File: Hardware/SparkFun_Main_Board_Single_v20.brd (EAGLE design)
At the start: 86.4 x 73.7 mm, 128 parts, among them J1 MICROMOD-2222-C, J10 MICRO-SD-PUSH-PUSH-EXT-PIN, J2 Vertical Qwiic Connector, J4 QWIIC_RIGHT_ANGLE, J5 CORTEX_JTAG_DEBUG_MINIMUM_PTH, J6 MICROMOD_FUNCTION_MAIN, Q1 3.1A/30V/105mΩ, Q2 20V/4.2A/52mΩ/1.4W, U1 STG3856QTR, U2 MCP73831, U3 ESD Diode, U4 AP7347DQ-33W5-7K-3.3V, U5 AP7361C-33

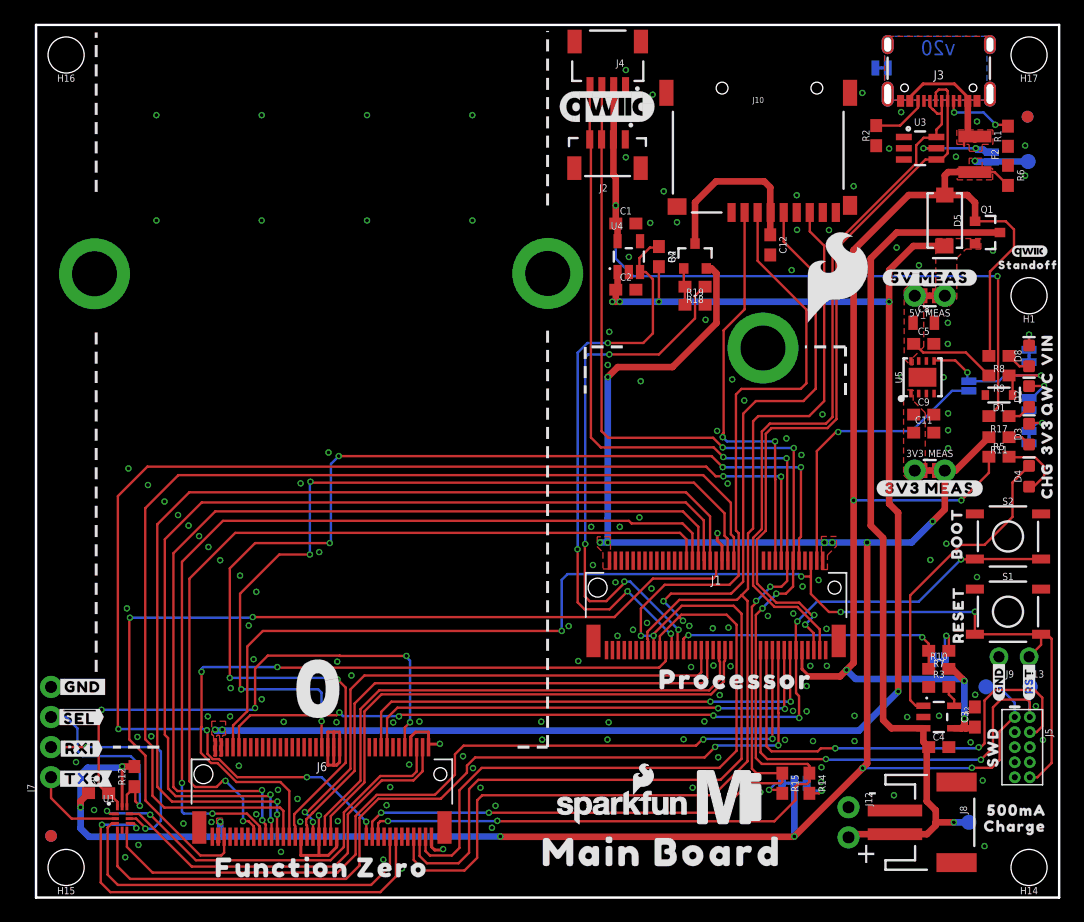
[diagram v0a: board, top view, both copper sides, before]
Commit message: Routes PWM1 pin to power enable pin on function card
* Rolls version to v21
* Fixes PTC silk
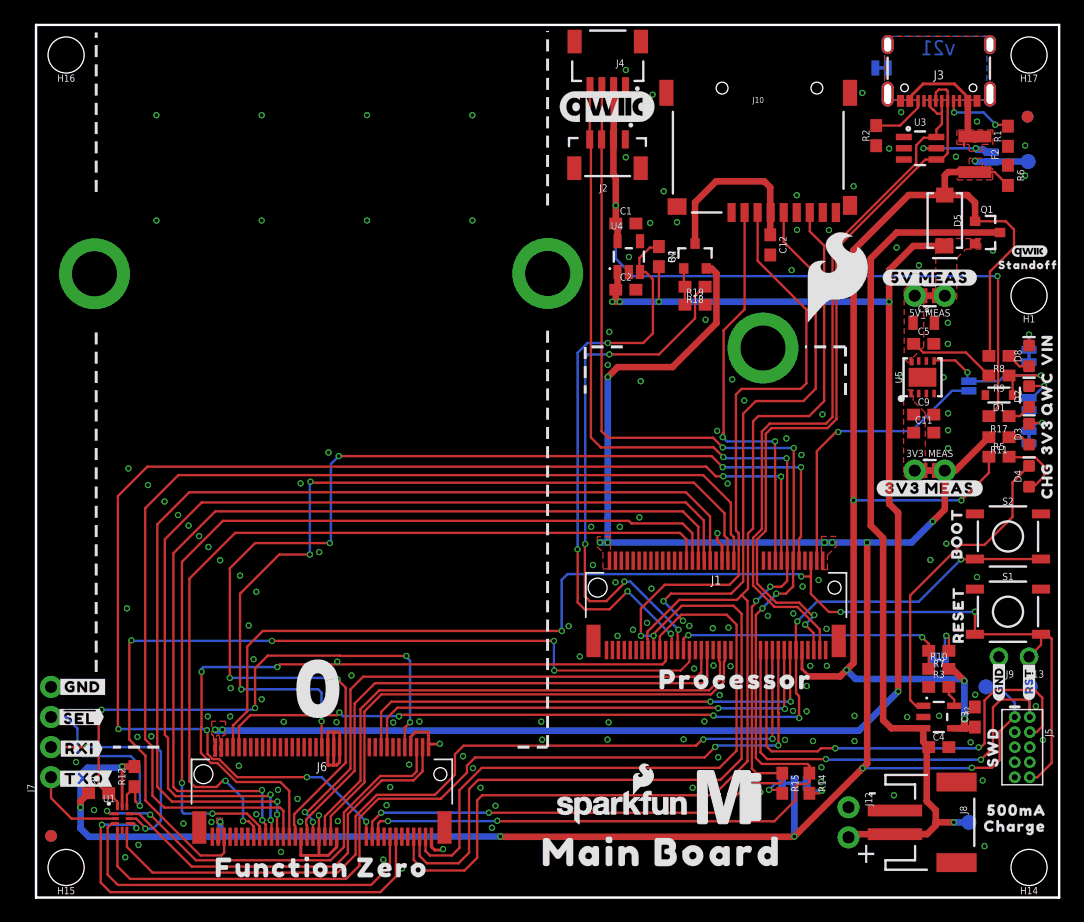
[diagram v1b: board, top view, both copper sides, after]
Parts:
- U$3: device top:#PTC#503 -> top:#PTC#15
- moved U$3 5.79 mm to (77.7, 62.5)
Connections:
- net PWR_EN0: now also J1.47; no longer J1.38
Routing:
- net PWR_EN0: track 78.2 -> 75.1 mm, vias 2 -> 4
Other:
- board text added: "v21"
- board text removed: "v20"
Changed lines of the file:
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@@
 <layer number="28" name="bValues" color="7" fill="1" visible="no" active="yes"/>
 <layer number="29" name="tStop" color="7" fill="3" visible="no" active="yes"/>
-<layer number="30" name="bStop" color="7" fill="6" visible="no" active="yes"/>
+<layer number="30" name="bStop" color="7" fill="6" visible="yes" active="yes"/>
 <layer number="31" name="tCream" color="7" fill="4" visible="no" active="yes"/>
 <layer number="32" name="bCream" color="7" fill="5" visible="no" active="yes"/>
@@
 <wire x1="0" y1="0" x2="0" y2="73.66" width="0.2032" layer="20"/>
 <wire x1="86.36" y1="0" x2="86.36" y2="73.66" width="0.2032" layer="20"/>
-<text x="76.1492" y="71.7296" size="1.27" layer="16" font="vector" ratio="15" rot="MR180" align="center">v20</text>
+<text x="76.1492" y="71.7296" size="1.27" layer="16" font="vector" ratio="15" rot="MR180" align="center">v21</text>
 <text x="43.18" y="-25.654" size="1.778" layer="51" font="vector">Elias Santistevan</text>
 <text x="50.673" y="-14.859" size="1.778" layer="47" font="vector" ratio="15" rot="R180">Units in Inches</text>
@@
 </element>
 <element name="U$27" library="top" package="CHARGE501" value="" x="82.6262" y="6.0198" smashed="yes"/>
-<element name="U$3" library="top" package="#PTC#503" value="" x="83.5152" y="62.5602" smashed="yes" rot="MR0"/>
 <element name="U$7" library="top" package="#SHLD#501" value="" x="74.8792" y="70.0532" smashed="yes" rot="MR0"/>
 <element name="5V_MEAS" library="SparkFun-Jumpers" package="COMBO-JUMPER_2_NC_TRACE" value="JUMPER-COMBO_2_NC_TRACE" x="75.438" y="50.8" smashed="yes" rot="R180">
@@
 <element name="U$20" library="bot" package="#RXI#4" value="" x="3.683" y="12.573" smashed="yes" rot="MR0"/>
 <element name="U$28" library="bot" package="#TXO#5" value="" x="4.064" y="10.033" smashed="yes" rot="MR0"/>
+<element name="U$3" library="top" package="#PTC#15" value="" x="77.724" y="62.484" smashed="yes" rot="MR0"/>
 </elements>
 <signals>
@@
 <via x="25.4762" y="6.4516" extent="1-16" drill="0.3048"/>
 <via x="22.3012" y="6.4008" extent="1-16" drill="0.3048"/>
-<via x="45.7708" y="19.9644" extent="1-16" drill="0.3048"/>
+<via x="45.8978" y="20.3454" extent="1-16" drill="0.3048"/>
 <via x="17.9578" y="22.9616" extent="1-16" drill="0.3048"/>
 <via x="16.4338" y="17.6784" extent="1-16" drill="0.3048"/>
@@
 <via x="7.6708" y="24.4094" extent="1-16" drill="0.3048"/>
 <via x="25.4254" y="19.9136" extent="1-16" drill="0.3048"/>
-<via x="55.2958" y="19.4564" extent="1-16" drill="0.3048"/>
+<via x="55.5498" y="19.3294" extent="1-16" drill="0.3048"/>
 <via x="8.64508125" y="4.445" extent="1-16" drill="0.3048"/>
 <via x="4.9022" y="7.3914" extent="1-16" drill="0.3048"/>
@@
 <contactref element="J1" pad="55"/>
 <wire x1="53.154" y1="19.9644" x2="53.154" y2="20.887" width="0.2032" layer="1"/>
-<wire x1="52.5952" y1="19.4056" x2="20.4216" y2="19.4056" width="0.2032" layer="1"/>
-<wire x1="20.4216" y1="19.4056" x2="20.3708" y2="19.4564" width="0.2032" layer="1"/>
+<wire x1="52.8746" y1="19.685" x2="20.5994" y2="19.685" width="0.2032" layer="1"/>
+<wire x1="20.3708" y1="19.4564" x2="20.5994" y2="19.685" width="0.2032" layer="1"/>
 <via x="20.3708" y="19.4564" extent="1-16" drill="0.3048"/>
 <wire x1="20.3708" y1="19.4564" x2="14.1224" y2="19.4564" width="0.2032" layer="16"/>
@@
 <wire x1="20.6248" y1="9.7536" x2="21.38" y2="8.9984" width="0.2032" layer="1"/>
 <wire x1="21.38" y1="8.9984" x2="21.38" y2="5.139" width="0.2032" layer="1"/>
-<wire x1="52.5952" y1="19.4056" x2="53.154" y2="19.9644" width="0.2032" layer="1"/>
+<wire x1="52.8746" y1="19.685" x2="53.154" y2="19.9644" width="0.2032" layer="1"/>
 <wire x1="13.97" y1="19.05" x2="13.97" y2="14.383625" width="0.2032" layer="1"/>
 <wire x1="13.97" y1="14.383625" x2="13.9192" y2="14.332825" width="0.2032" layer="1"/>
@@
 <signal name="PROCESSOR_CAN-TX">
 <contactref element="J1" pad="43"/>
-<wire x1="27.7154875" y1="18.7452" x2="55.88" y2="18.7452" width="0.2032" layer="1"/>
-<wire x1="27.7154875" y1="18.7452" x2="26.543" y2="17.5727125" width="0.2032" layer="1"/>
+<wire x1="27.6138875" y1="18.6436" x2="55.7784" y2="18.6436" width="0.2032" layer="1"/>
+<wire x1="27.6138875" y1="18.6436" x2="26.543" y2="17.5727125" width="0.2032" layer="1"/>
 <wire x1="22.8854" y1="7.2136" x2="22.6902" y2="7.2136" width="0.2032" layer="1"/>
 <wire x1="26.543" y1="10.8712" x2="22.8854" y2="7.2136" width="0.2032" layer="1"/>
@@
 <wire x1="22.6902" y1="7.2136" x2="23.368" y2="6.5358" width="0.2032" layer="16"/>
 <wire x1="23.368" y1="6.5358" x2="23.368" y2="6.3754" width="0.2032" layer="16"/>
-<wire x1="55.88" y1="18.7452" x2="56.154" y2="19.0192" width="0.2032" layer="1"/>
+<wire x1="55.7784" y1="18.6436" x2="56.154" y2="19.0192" width="0.2032" layer="1"/>
 </signal>
 <signal name="SWDIO">
@@
 </signal>
 <signal name="PWR_EN0">
-<contactref element="J1" pad="38"/>
 <contactref element="J6" pad="71"/>
-<wire x1="57.404" y1="28.437" x2="57.404" y2="27.178" width="0.2032" layer="1"/>
-<wire x1="57.404" y1="27.178" x2="57.15" y2="26.924" width="0.2032" layer="1"/>
-<wire x1="57.15" y1="26.924" x2="52.07" y2="26.924" width="0.2032" layer="1"/>
-<wire x1="52.07" y1="26.924" x2="48.8188" y2="23.6728" width="0.2032" layer="1"/>
-<wire x1="48.8188" y1="23.6728" x2="18.288" y2="23.6728" width="0.2032" layer="1"/>
-<via x="18.288" y="23.6728" extent="1-16" drill="0.3048"/>
-<wire x1="18.288" y1="23.6728" x2="18.2372" y2="23.622" width="0.2032" layer="16"/>
-<wire x1="18.2372" y1="23.622" x2="7.9248" y2="23.622" width="0.2032" layer="16"/>
-<via x="7.9248" y="23.622" extent="1-16" drill="0.3048"/>
-<wire x1="7.9248" y1="23.622" x2="7.874" y2="23.5712" width="0.2032" layer="1"/>
-<wire x1="7.874" y1="23.5712" x2="7.874" y2="13.3446" width="0.2032" layer="1"/>
+<via x="19.9136" y="21.6662" extent="1-16" drill="0.3048"/>
+<wire x1="43.7134" y1="21.6662" x2="19.9136" y2="21.6662" width="0.2032" layer="1"/>
+<wire x1="19.9136" y1="21.6662" x2="8.1026" y2="21.6662" width="0.2032" layer="16"/>
+<wire x1="8.1026" y1="21.6662" x2="8.0518" y2="21.717" width="0.2032" layer="16"/>
+<via x="8.0518" y="21.717" extent="1-16" drill="0.3048"/>
+<wire x1="8.0518" y1="21.717" x2="7.874" y2="21.5392" width="0.2032" layer="1"/>
+<wire x1="7.874" y1="21.5392" x2="7.874" y2="13.3446" width="0.2032" layer="1"/>
 <wire x1="7.874" y1="13.3446" x2="9.2376" y2="11.981" width="0.2032" layer="1"/>
 <wire x1="9.2376" y1="11.981" x2="9.2376" y2="8.1868" width="0.2032" layer="1"/>
@@
 <wire x1="15.88" y1="3.7896" x2="15.88" y2="5.139" width="0.2032" layer="1"/>
 <wire x1="13.86783125" y1="3.556" x2="15.6464" y2="3.556" width="0.2032" layer="1"/>
+<contactref element="J1" pad="47"/>
+<wire x1="55.154" y1="20.887" x2="55.1469" y2="20.8799" width="0.1778" layer="1"/>
+<wire x1="55.1469" y1="20.8799" x2="55.1469" y2="19.89556875" width="0.1778" layer="1"/>
+<wire x1="55.1469" y1="19.89556875" x2="54.41563125" y2="19.1643" width="0.1778" layer="1"/>
+<wire x1="54.41563125" y1="19.1643" x2="43.7388" y2="19.1643" width="0.1778" layer="1"/>
+<via x="43.7388" y="19.1643" extent="1-16" drill="0.3048"/>
+<via x="43.7134" y="21.6662" extent="1-16" drill="0.3048"/>
+<wire x1="43.7388" y1="19.1643" x2="43.7134" y2="19.1897" width="0.1778" layer="16"/>
+<wire x1="43.7134" y1="19.1897" x2="43.7134" y2="21.6662" width="0.1778" layer="16"/>
 </signal>
 <signal name="N$7">

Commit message: Rotates JST connector, fixes some silk labels
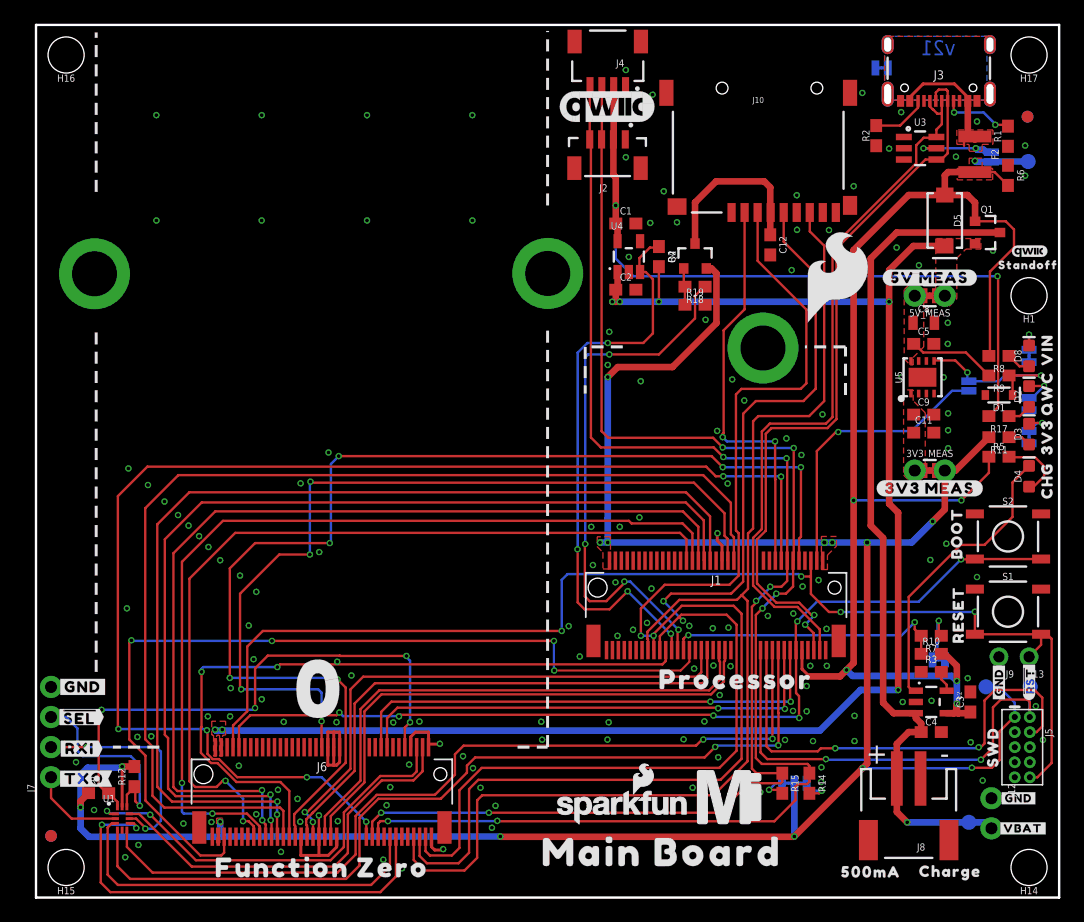
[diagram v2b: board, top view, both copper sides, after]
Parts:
- removed U$40: (no value), top:#GND#6520
- added U$36, U$37: (no value), top:#GND#10
- added U$38: (no value), top:##RST##8
- U$39: device top:#RST#6521 -> top:#VBAT#9
- moved U$33 13.4 mm to (70.5, 2.16)
- moved U$39 12.5 mm to (83.3, 5.84), turned to 0 degrees
- moved J12 12.1 mm to (80.6, 8.38)
- moved U$27 6.66 mm to (77.2, 2.21)
- moved J8 2.54 mm to (73.7, 6.35), turned to 180 degrees
- moved R10 1.42 mm to (75.6, 20.6)
- moved C4 1.42 mm to (75.6, 14.0)
- moved U2 1.42 mm to (75.6, 16.5)
- moved R3 1.42 mm to (75.6, 19.1)
- moved R7 1.42 mm to (75.6, 22.1)
- moved C3 1.33 mm to (78.9, 16.5)
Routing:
- net V_BATT: track 74.2 -> 71.7 mm
- net N$8: track 26.4 -> 24.8 mm
- net N$7: track 3.54 -> 5.05 mm
- net GND: vias 160 -> 158

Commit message: Moves JST connector in 0.1"
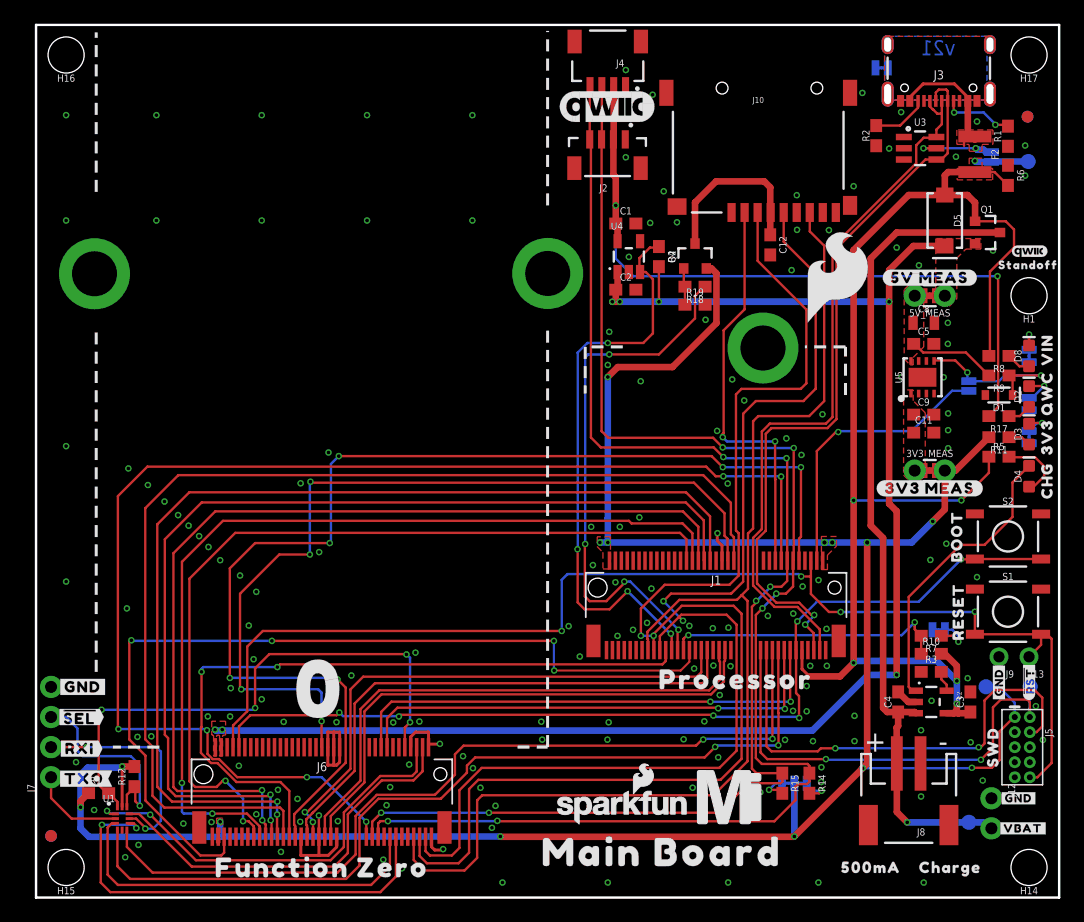
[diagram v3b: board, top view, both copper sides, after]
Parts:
- moved C4 3.78 mm to (72.8, 16.5), turned to 90 degrees
- moved DIVIDER 2.54 mm to (76.2, 22.6)
- moved U$52 2.54 mm to (71.6, 22.5)
- moved J8 1.27 mm to (73.7, 7.62)
- moved U$33 0.38 mm to (70.5, 2.54)
- moved U$27 0.33 mm to (77.2, 2.54)
- moved U$8 0.25 mm to (77.7, 30.5)
- moved U$9 0.25 mm to (77.9, 24.1)
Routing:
- net GND: track 28.7 -> 30.5 mm, vias 158 -> 168
- net N$7: track 5.05 -> 3.50 mm
- net V_BATT: track 71.7 -> 70.2 mm
- net VCC: track 130.0 -> 129.0 mm
- net VIN: track 115.0 -> 114.1 mm

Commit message: Adds notch for batteries, moves VBAT test point
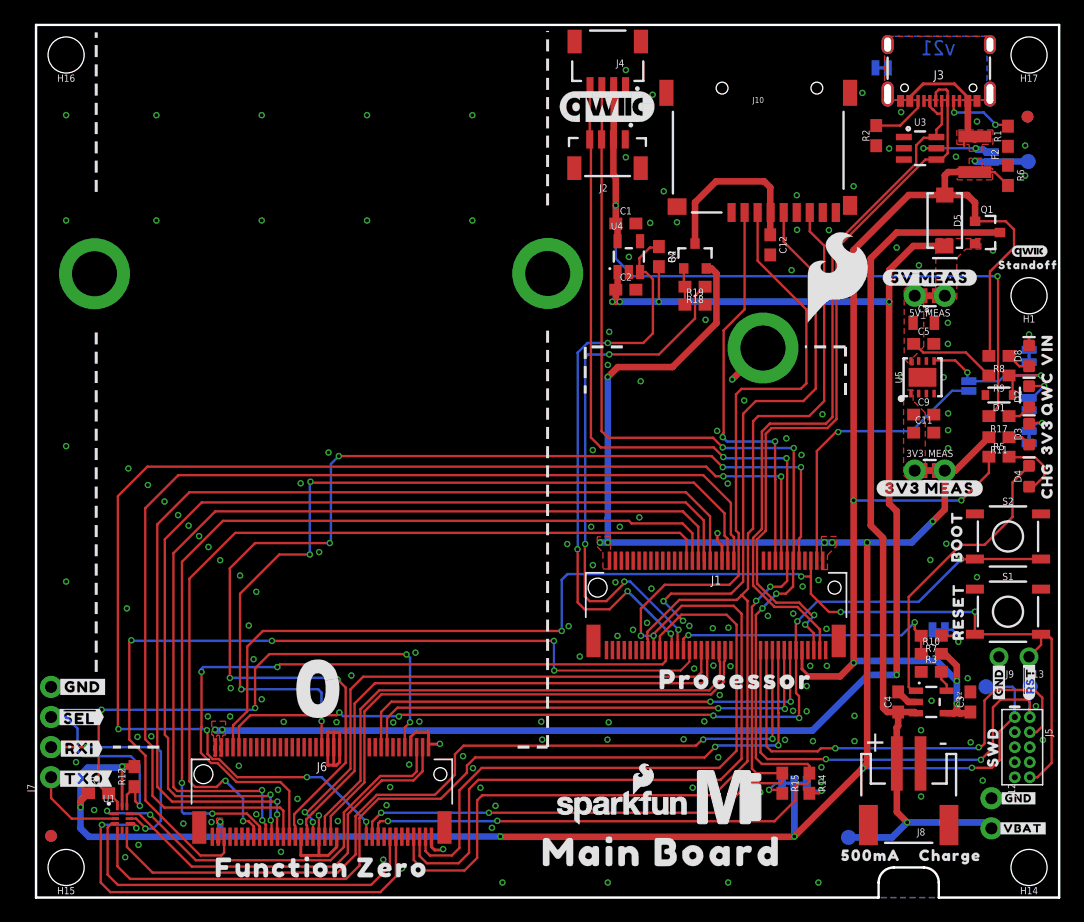
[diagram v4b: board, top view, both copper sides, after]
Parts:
- moved TP3 10.2 mm to (68.6, 5.08)
- moved FRAME1 6.35 mm to (16.5, -31.8)
- moved FRAME2 6.35 mm to (16.5, -31.8)
- moved U$27 1.02 mm to (77.2, 3.56)
- moved U$33 1.02 mm to (70.5, 3.56)
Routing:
- net V_BATT: track 70.2 -> 75.7 mm
- net GND: track 30.5 -> 34.2 mm, vias 168 -> 169
- net 3.3V: track 197.6 -> 198.3 mm
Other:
- outline, holes or cut-outs redrawn
